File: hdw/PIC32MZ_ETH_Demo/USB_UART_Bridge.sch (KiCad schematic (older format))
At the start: 28 parts

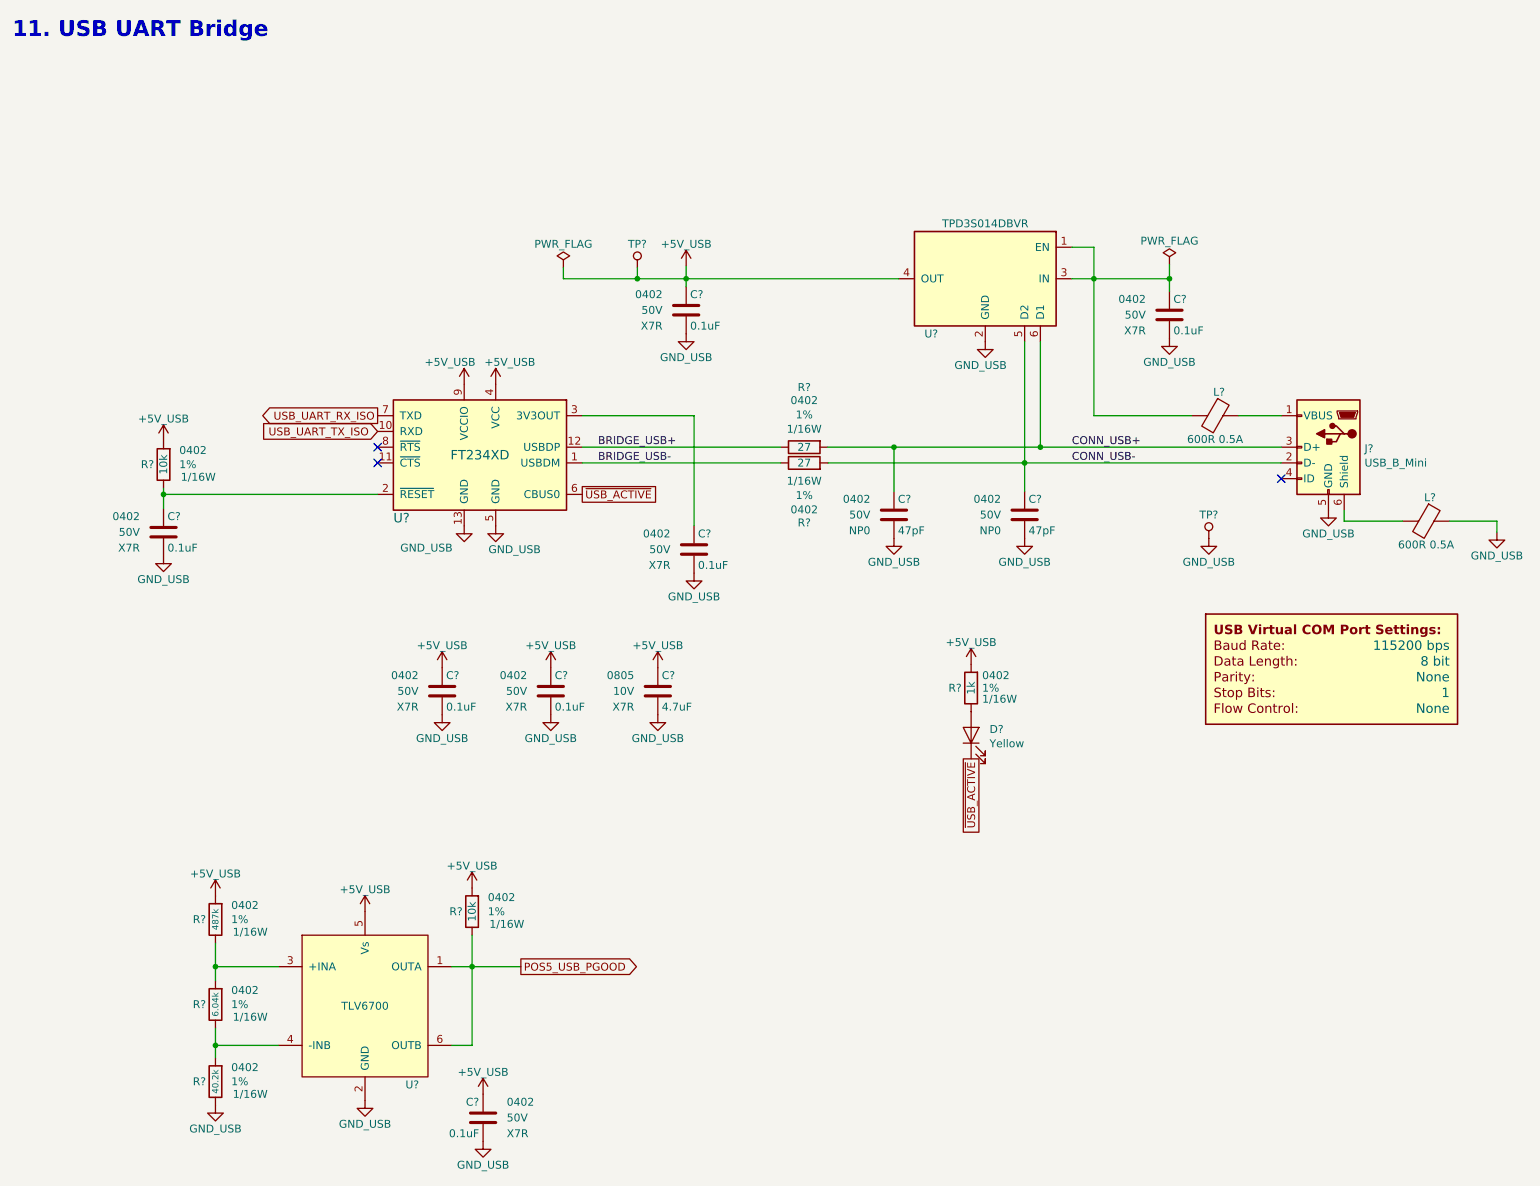
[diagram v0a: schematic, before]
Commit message: More schematic tweaks, followed PHY design guide
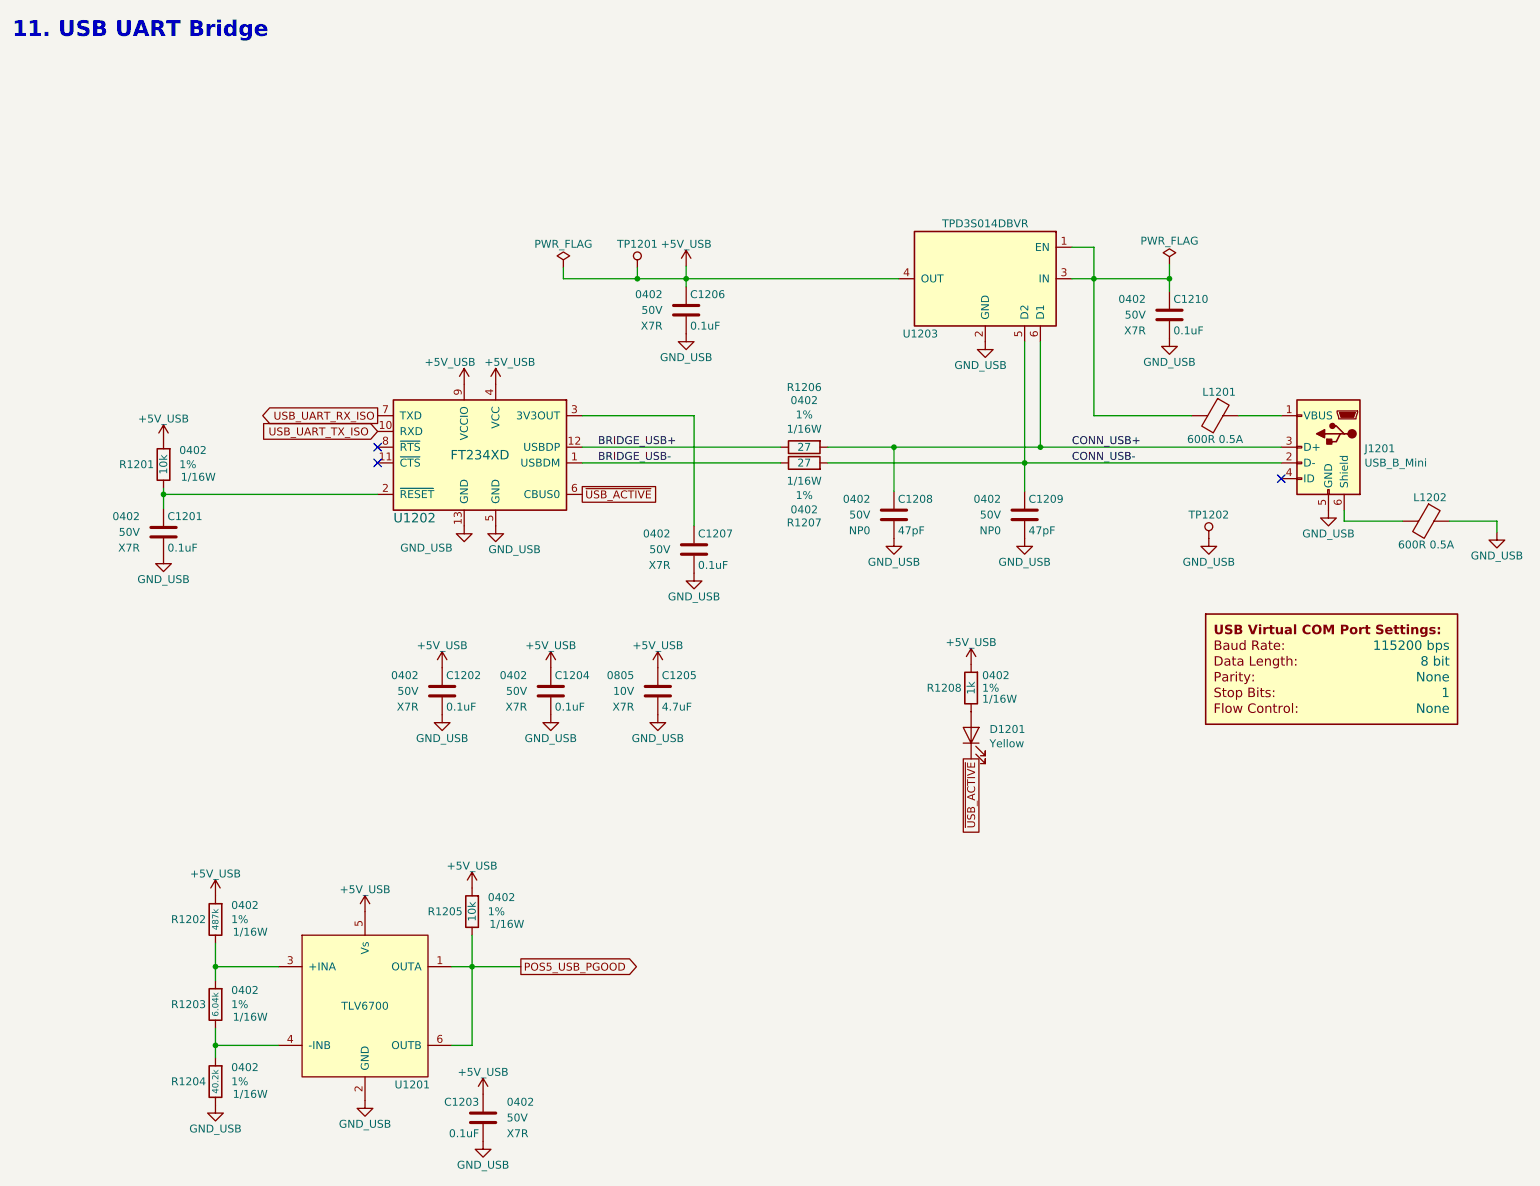
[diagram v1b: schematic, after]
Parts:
- gave numbers to parts that had none: 28

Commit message: Populated digi-key pn's
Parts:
- C1201, C1202, C1203, C1204, C1206, C1207, C1210: Digi-Key PN (none) -> 490-10701-1-ND
- C1208, C1209: Digi-Key PN (none) -> 399-17558-1-ND
- D1201: footprint LEDs:LED_0603 -> LEDs:LED_0402; Digi-Key PN (none) -> 1497-1389-1-ND
- L1201, L1202: footprint Inductors_SMD:L_0603 -> Inductors_SMD:L_0402; Digi-Key PN (none) -> 490-5441-1-ND
- R1201, R1205: Digi-Key PN (none) -> RMCF0402FT10K0CT-ND
- R1202: Digi-Key PN (none) -> RMCF0402FT487KCT-ND
- R1203: Digi-Key PN (none) -> 541-4067-1-ND
- R1204: Digi-Key PN (none) -> 541-4097-1-ND
- R1206, R1207: Digi-Key PN (none) -> 541-4082-1-ND
- R1208: Digi-Key PN (none) -> 541-1.00KLCT-ND
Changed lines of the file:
@@
 F 5 "50V" H 6000 3720 50  0000 R CNN "Voltage"
 F 6 "NP0" H 6000 3620 50  0000 R CNN "Dielectric"
-F 7 "" H 6575 4220 60  0001 C CNN "Digi-Key PN"
+F 7 "399-17558-1-ND" H 6575 4220 60  0001 C CNN "Digi-Key PN"
 	1    6150 3720
 	1    0    0    -1
@@
 F 5 "50V" H 3820 4840 50  0000 R CNN "Voltage"
 F 6 "X7R" H 3820 4740 50  0000 R CNN "Dielectric"
-F 7 "" H 4395 5340 60  0001 C CNN "Digi-Key PN"
+F 7 "490-10701-1-ND" H 4395 5340 60  0001 C CNN "Digi-Key PN"
 	1    3970 4840
 	1    0    0    -1
@@
 F 5 "50V" H 1360 3830 50  0000 R CNN "Voltage"
 F 6 "X7R" H 1360 3730 50  0000 R CNN "Dielectric"
-F 7 "" H 1935 4330 60  0001 C CNN "Digi-Key PN"
+F 7 "490-10701-1-ND" H 1935 4330 60  0001 C CNN "Digi-Key PN"
 	1    1510 3830
 	1    0    0    -1
@@
 F 5 "1%" H 1610 3400 50  0000 L CNN "Tolerance"
 F 6 "1/16W" H 1620 3320 50  0000 L CNN "Wattage"
-F 7 "" H 1810 3800 60  0001 C CNN "Digi-Key PN"
+F 7 "RMCF0402FT10K0CT-ND" H 1810 3800 60  0001 C CNN "Digi-Key PN"
 	1    1510 3400
 	1    0    0    -1
@@
 F 5 "50V" H 6830 3720 50  0000 R CNN "Voltage"
 F 6 "NP0" H 6830 3620 50  0000 R CNN "Dielectric"
-F 7 "" H 7405 4220 60  0001 C CNN "Digi-Key PN"
+F 7 "399-17558-1-ND" H 7405 4220 60  0001 C CNN "Digi-Key PN"
 	1    6980 3720
 	1    0    0    -1
@@
 F 5 "50V" H 3130 4840 50  0000 R CNN "Voltage"
 F 6 "X7R" H 3130 4740 50  0000 R CNN "Dielectric"
-F 7 "" H 3705 5340 60  0001 C CNN "Digi-Key PN"
+F 7 "490-10701-1-ND" H 3705 5340 60  0001 C CNN "Digi-Key PN"
 	1    3280 4840
 	1    0    0    -1
@@
 F 5 "50V" H 4730 3940 50  0000 R CNN "Voltage"
 F 6 "X7R" H 4730 3840 50  0000 R CNN "Dielectric"
-F 7 "" H 5305 4440 60  0001 C CNN "Digi-Key PN"
+F 7 "490-10701-1-ND" H 5305 4440 60  0001 C CNN "Digi-Key PN"
 	1    4880 3940
 	1    0    0    -1
@@
 F 5 "50V" H 7750 2450 50  0000 R CNN "Voltage"
 F 6 "X7R" H 7750 2350 50  0000 R CNN "Dielectric"
-F 7 "" H 8325 2950 60  0001 C CNN "Digi-Key PN"
+F 7 "490-10701-1-ND" H 8325 2950 60  0001 C CNN "Digi-Key PN"
 	1    7900 2450
 	1    0    0    -1
@@
 F 5 "50V" H 4680 2420 50  0000 R CNN "Voltage"
 F 6 "X7R" H 4680 2320 50  0000 R CNN "Dielectric"
-F 7 "" H 5255 2920 60  0001 C CNN "Digi-Key PN"
+F 7 "490-10701-1-ND" H 5255 2920 60  0001 C CNN "Digi-Key PN"
 	1    4830 2420
 	1    0    0    -1
@@
 F 5 "1%" H 6710 4820 50  0000 L CNN "Tolerance"
 F 6 "1/16W" H 6710 4750 50  0000 L CNN "Wattage"
-F 7 "" H 6940 5220 60  0001 C CNN "Digi-Key PN"
+F 7 "541-1.00KLCT-ND" H 6940 5220 60  0001 C CNN "Digi-Key PN"
 	1    6640 4820
 	1    0    0    -1
@@
 F 0 "L1201" V 8040 3115 50  0000 C CNN
 F 1 "600R 0.5A" V 8340 3090 50  0000 C CNN
-F 2 "Inductors_SMD:L_0603" V 8120 3090 50  0001 C CNN
+F 2 "Inductors_SMD:L_0402" V 8120 3090 50  0001 C CNN
 F 3 "~" H 8190 3090 50  0001 C CNN
-F 4 "" H 0   0   50  0001 C CNN "Digi-Key PN"
+F 4 "490-5441-1-ND" H 0   0   50  0001 C CNN "Digi-Key PN"
 	1    8190 3090
 	0    1    1    0
@@
 F 5 "1%" V 5786 3290 50  0000 C CNN "Tolerance"
 F 6 "1/16W" V 5695 3290 50  0000 C CNN "Wattage"
-F 7 "" H 5880 3690 60  0001 C CNN "Digi-Key PN"
+F 7 "541-4082-1-ND" H 5880 3690 60  0001 C CNN "Digi-Key PN"
 	1    5580 3290
 	0    1    -1   0
@@
 F 0 "D1201" V 6678 5003 50  0000 R CNN
 F 1 "Yellow" V 6587 5003 50  0000 R CNN
-F 2 "LEDs:LED_0603" H 6640 5120 50  0001 C CNN
+F 2 "LEDs:LED_0402" H 6640 5120 50  0001 C CNN
 F 3 "~" H 6640 5120 50  0001 C CNN
-F 4 "" H 0   0   50  0001 C CNN "Digi-Key PN"
+F 4 "1497-1389-1-ND" H 0   0   50  0001 C CNN "Digi-Key PN"
 	1    6640 5120
 	0    -1   -1   0
@@
 F 0 "L1202" V 9380 3785 50  0000 C CNN
 F 1 "600R 0.5A" V 9680 3760 50  0000 C CNN
-F 2 "Inductors_SMD:L_0603" V 9460 3760 50  0001 C CNN
+F 2 "Inductors_SMD:L_0402" V 9460 3760 50  0001 C CNN
 F 3 "~" H 9530 3760 50  0001 C CNN
-F 4 "" H 0   0   50  0001 C CNN "Digi-Key PN"
+F 4 "490-5441-1-ND" H 0   0   50  0001 C CNN "Digi-Key PN"
 	1    9530 3760
 	0    1    1    0
@@
 F 5 "1%" H 1940 6830 50  0000 L CNN "Tolerance"
 F 6 "1/16W" H 1950 6750 50  0000 L CNN "Wattage"
-F 7 "" H 2140 7230 60  0001 C CNN "Digi-Key PN"
+F 7 "541-4067-1-ND" H 2140 7230 60  0001 C CNN "Digi-Key PN"
 	1    1840 6830
 	1    0    0    -1
@@
 F 5 "1%" H 1940 7320 50  0000 L CNN "Tolerance"
 F 6 "1/16W" H 1950 7240 50  0000 L CNN "Wattage"
-F 7 "" H 2140 7720 60  0001 C CNN "Digi-Key PN"
+F 7 "541-4097-1-ND" H 2140 7720 60  0001 C CNN "Digi-Key PN"
 	1    1840 7320
 	1    0    0    -1
@@
 F 5 "1%" H 1940 6290 50  0000 L CNN "Tolerance"
 F 6 "1/16W" H 1950 6210 50  0000 L CNN "Wattage"
-F 7 "" H 2140 6690 60  0001 C CNN "Digi-Key PN"
+F 7 "RMCF0402FT487KCT-ND" H 2140 6690 60  0001 C CNN "Digi-Key PN"
 	1    1840 6290
 	1    0    0    -1
@@
 F 5 "1%" H 3570 6240 50  0000 L CNN "Tolerance"
 F 6 "1/16W" H 3580 6160 50  0000 L CNN "Wattage"
-F 7 "" H 3770 6640 60  0001 C CNN "Digi-Key PN"
+F 7 "RMCF0402FT10K0CT-ND" H 3770 6640 60  0001 C CNN "Digi-Key PN"
 	1    3470 6240
 	1    0    0    -1
@@
 F 2 "Capacitors_SMD:C_0402" H 3578 7400 50  0001 C CNN
 F 3 "" H 3565 7650 50  0001 C CNN
-F 4 "" H 3965 8050 60  0001 C CNN "Digi-Key PN"
+F 4 "490-10701-1-ND" H 3965 8050 60  0001 C CNN "Digi-Key PN"
 F 5 "0402" H 3390 7650 50  0000 R CNN "display_footprint"
 F 6 "50V" H 3390 7550 50  0000 R CNN "Voltage"
@@
 F 5 "1%" V 5786 3390 50  0000 C CNN "Tolerance"
 F 6 "1/16W" V 5695 3390 50  0000 C CNN "Wattage"
-F 7 "" H 5880 3790 60  0001 C CNN "Digi-Key PN"
+F 7 "541-4082-1-ND" H 5880 3790 60  0001 C CNN "Digi-Key PN"
 	1    5580 3390
 	0    1    1    0

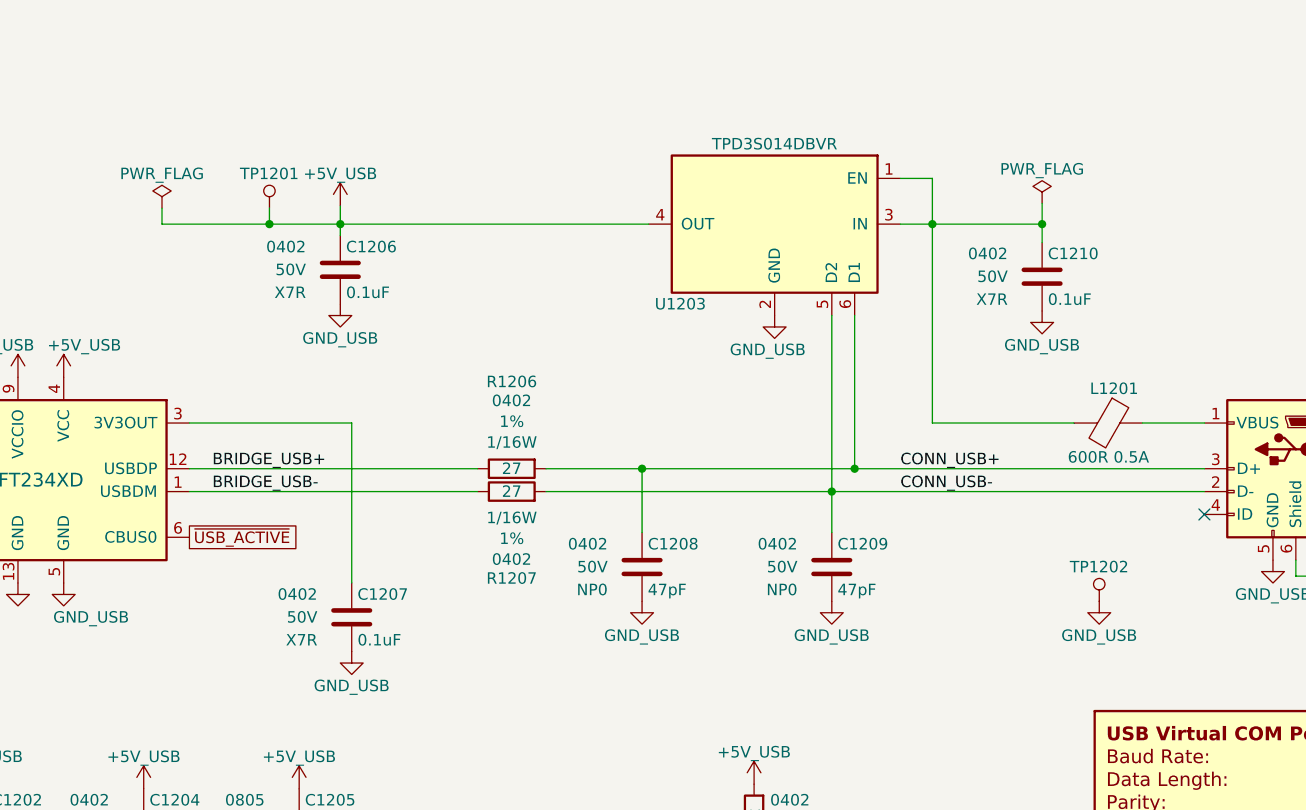
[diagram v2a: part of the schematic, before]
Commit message: Started arranging parts on PCB
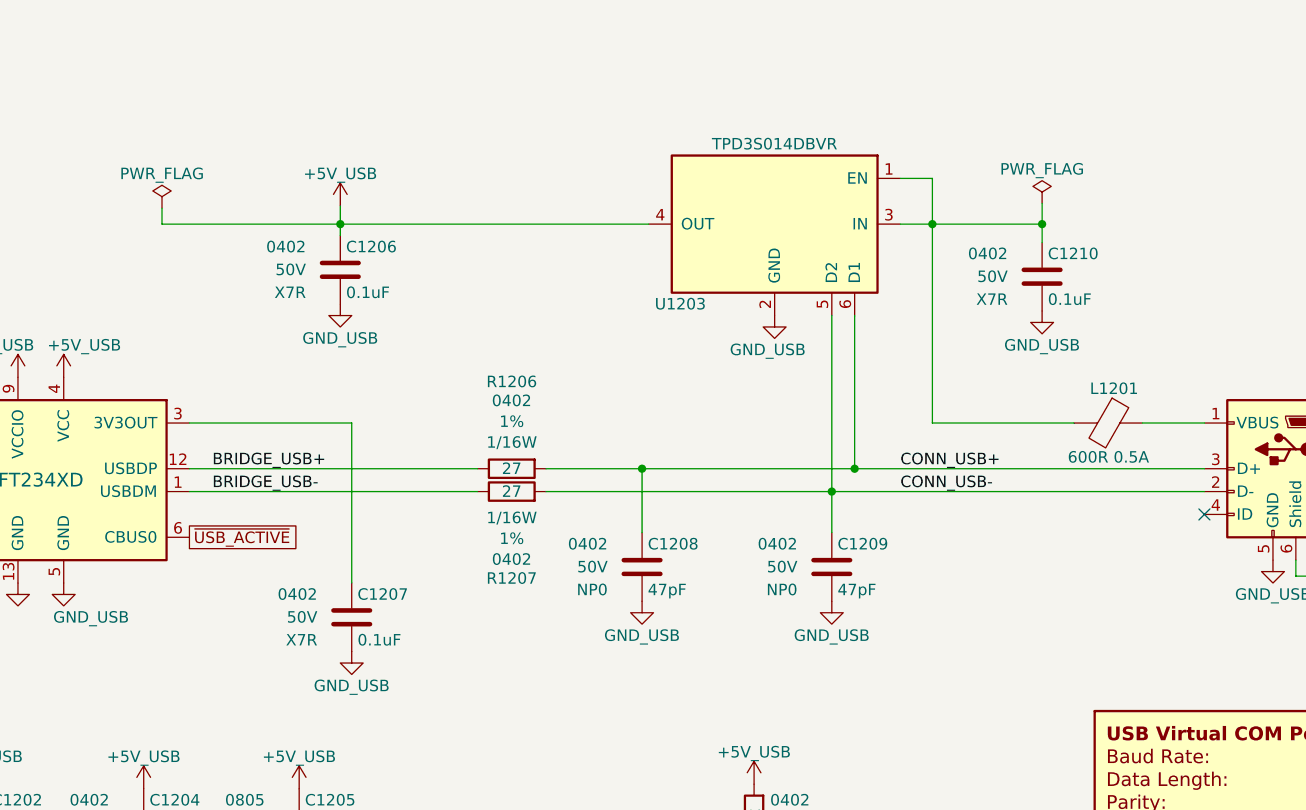
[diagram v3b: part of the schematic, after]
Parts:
- removed TP1201: TP, Custom Footprints Library:Test_Point, symbol Custom_Library:TP
- removed TP1202: TP, Pin_Headers:Pin_Header_Angled_1x01_Pitch2.54mm, symbol Custom_Library:TP
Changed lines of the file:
@@
-$EndComp
-$Comp
-L Custom_Library:TP TP?
-U 1 1 5E3059D8
-P 4520 2150
-AR Path="/5A557C58/5E3059D8" Ref="TP?"  Part="1"
-AR Path="/5A0BC776/5E3059D8" Ref="TP?"  Part="1"
-AR Path="/5CAD2D97/5E3059D8" Ref="TP?"  Part="1"
-AR Path="/5E6979AC/5E3059D8" Ref="TP1201"  Part="1"
-F 0 "TP1201" H 4520 2300 50  0000 C CNN
-F 1 "TP" H 4520 2300 50  0001 C CNN
-F 2 "Custom Footprints Library:Test_Point" H 4520 2150 60  0001 C CNN
-F 3 "" H 4520 2150 60  0000 C CNN
-	1    4520 2150
-	1    0    0    -1
-$EndComp
-Wire Wire Line
-	4520 2150 4520 2220
-Wire Wire Line
-	4520 2220 4830 2220
-$Comp
-L Custom_Library:TP TP?
-U 1 1 5E30EC63
-P 8150 3870
-AR Path="/5C1D5CD8/5E30EC63" Ref="TP?"  Part="1"
-AR Path="/5C1D5C9E/5E30EC63" Ref="TP?"  Part="1"
-AR Path="/5CB6F1ED/5E30EC63" Ref="TP?"  Part="1"
-AR Path="/5CAD2D97/5E30EC63" Ref="TP?"  Part="1"
-AR Path="/5E6979AC/5E30EC63" Ref="TP1202"  Part="1"
-F 0 "TP1202" H 8150 4020 50  0000 C CNN
-F 1 "TP" H 8150 4020 50  0001 C CNN
-F 2 "Pin_Headers:Pin_Header_Angled_1x01_Pitch2.54mm" H 8150 3870 60  0001 C CNN
-F 3 "" H 8150 3870 60  0000 C CNN
-	1    8150 3870
-	1    0    0    -1
-$EndComp
-$Comp
-L Custom_Library:GND_USB #PWR01228
-U 1 1 5E30F7F2
-P 8150 3870
-F 0 "#PWR01228" H 8150 3620 50  0001 C CNN
-F 1 "GND_USB" H 8150 3720 50  0000 C CNN
-F 2 "" H 8150 3870 50  0001 C CNN
-F 3 "" H 8150 3870 50  0001 C CNN
-	1    8150 3870
-	1    0    0    -1
 $EndComp
 $Comp
@@
 	4050 2150 4050 2220
 Wire Wire Line
-	4050 2220 4520 2220
-Connection ~ 4520 2220
-Wire Wire Line
 	7900 2300 7900 2220
 Connection ~ 7900 2220
 Wire Wire Line
 	6180 2220 4830 2220
+Wire Wire Line
+	4050 2220 4830 2220
 $EndSCHEMATC
